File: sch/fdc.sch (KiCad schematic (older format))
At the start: 22 parts, among them X4 SLOT-34

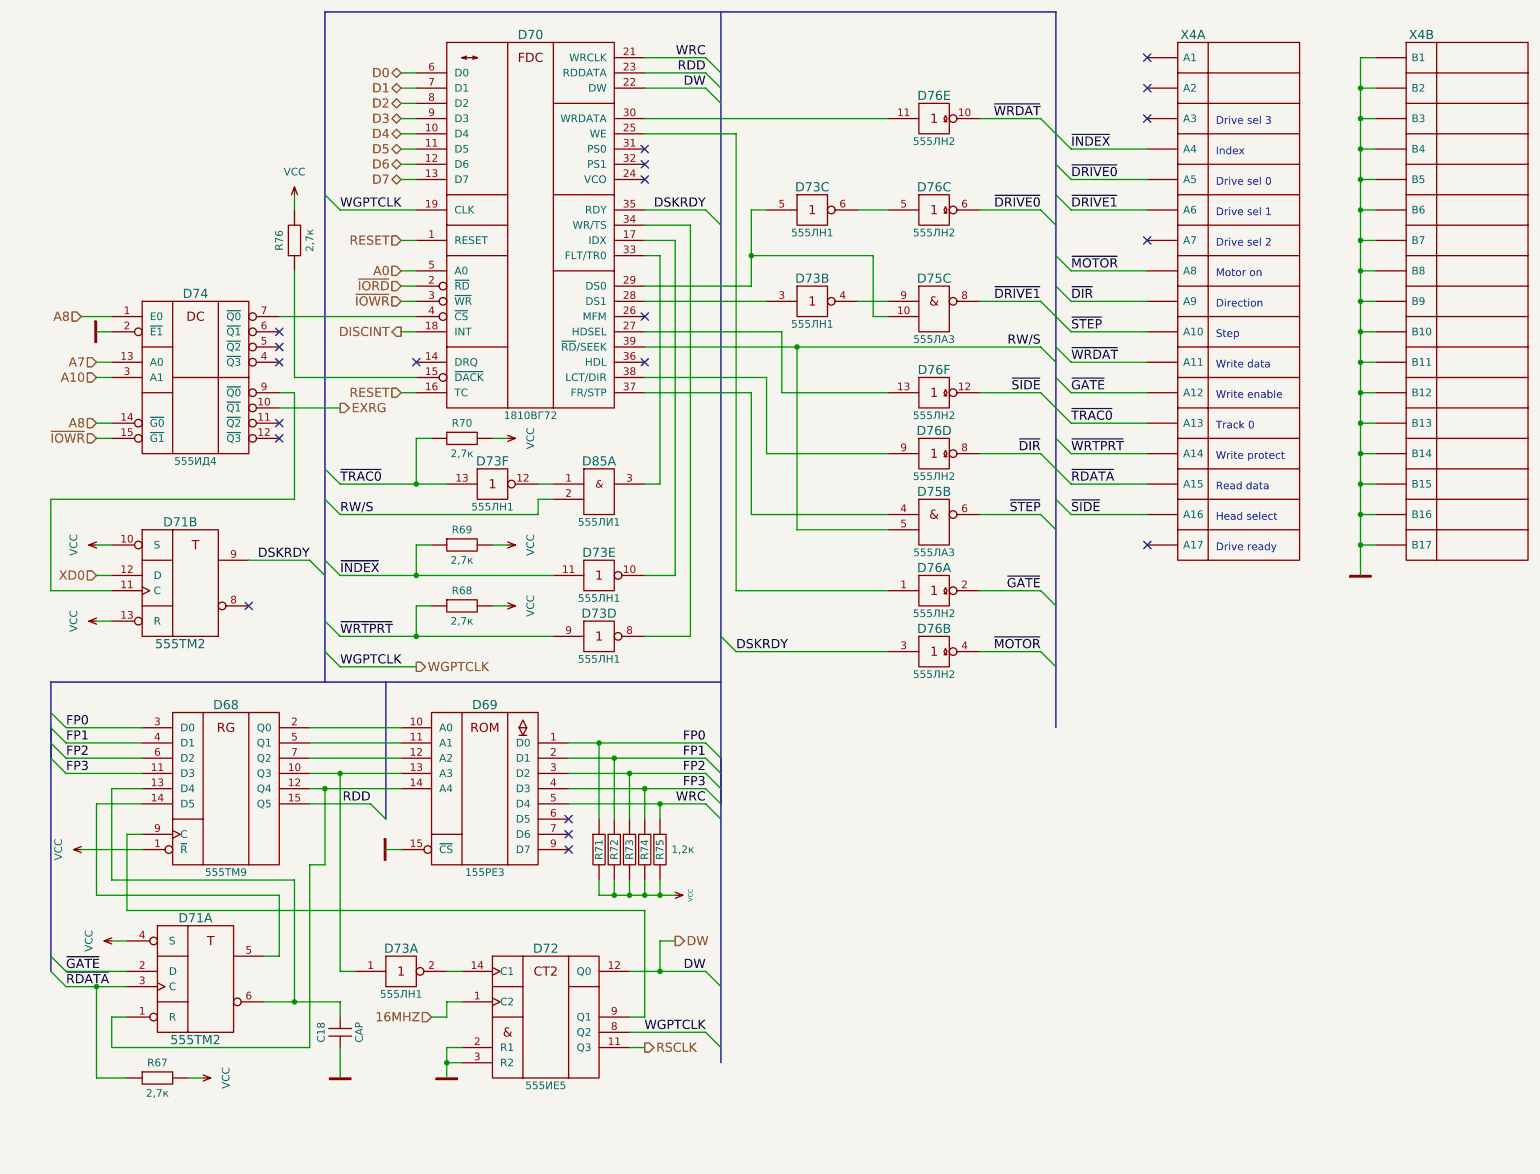
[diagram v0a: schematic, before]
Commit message: More precise version. PCB needs a lot of work.
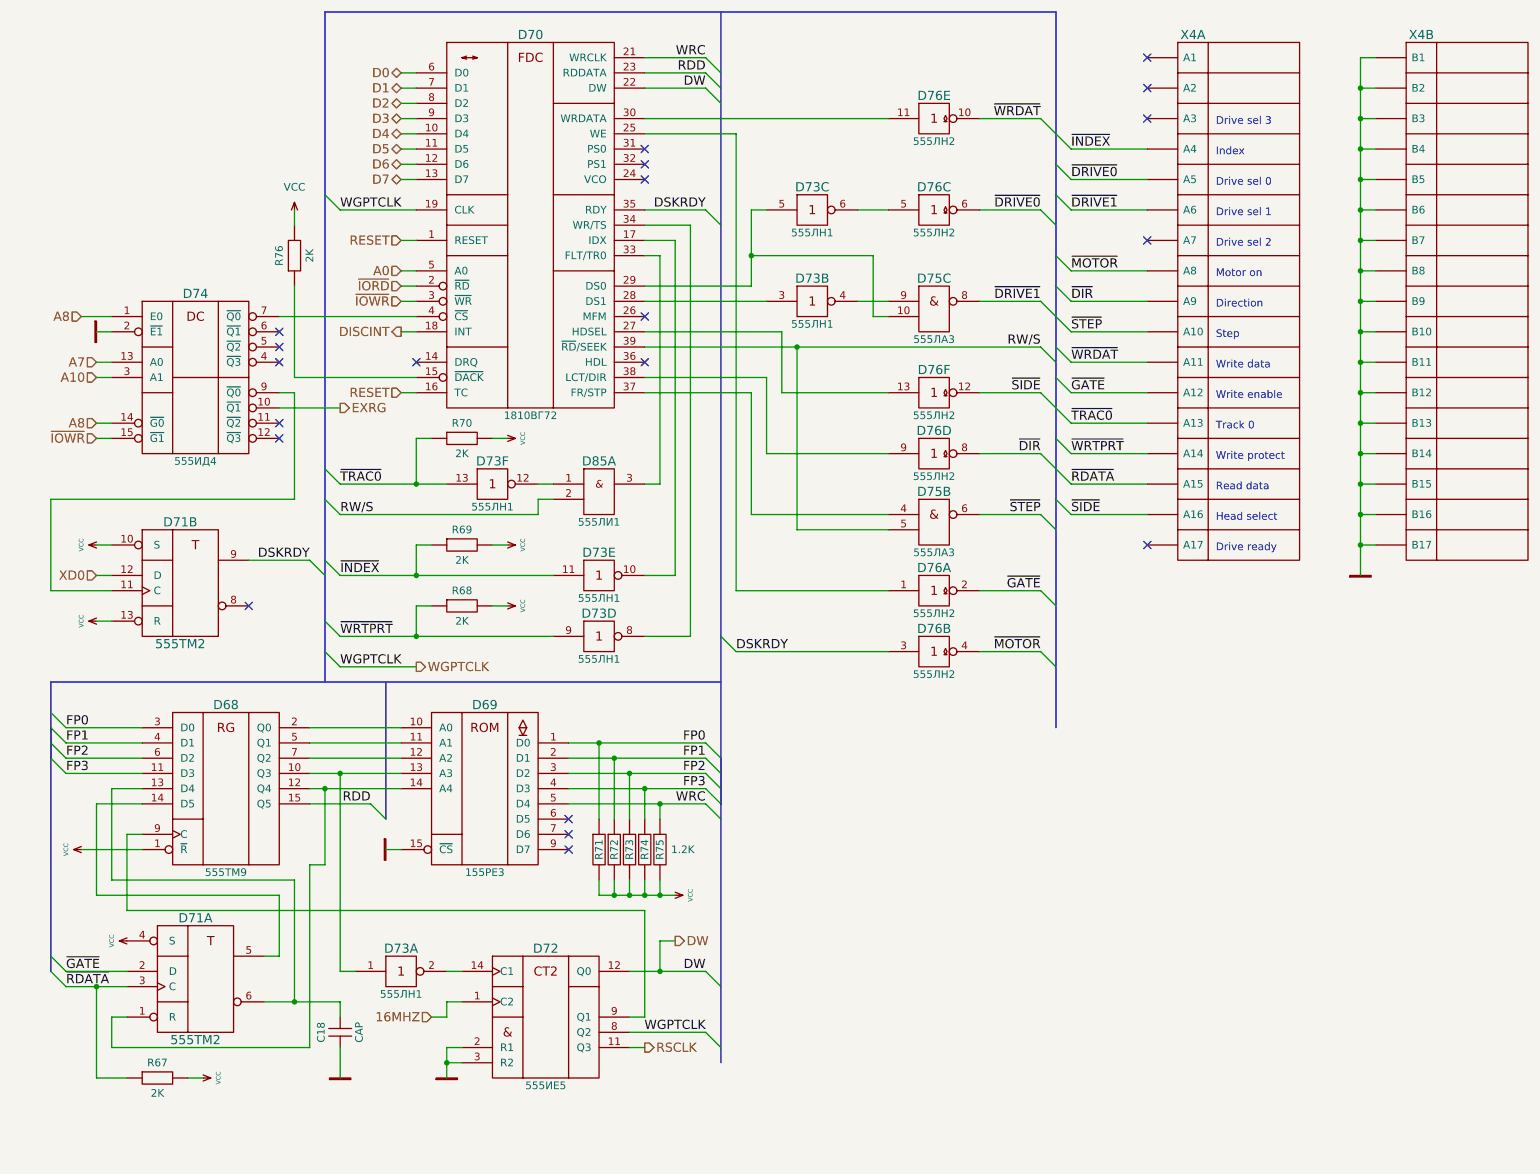
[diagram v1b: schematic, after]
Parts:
- C18: footprint MyLib:C_Disc_D7.5_P2.5 -> MyLib_metric:C_Disc_D7.5_P2.5
- D68, D69, D74: footprint MyLib:DIP-16 -> MyLib_metric:DIP-16
- D70: footprint MyLib:DIP-40 -> MyLib_metric:DIP-40
- D71, D72, D73, D75, D76, D85: footprint MyLib:DIP-14 -> MyLib_metric:DIP-14
- R67, R68, R69, R70: value 2,7к -> 2K; footprint MyLib:Resistor_Vertical_RM2.5mm -> MyLib_metric:Resistor_Vertical_RM2.5mm
- R71, R72, R73, R74, R75: value 1,2к -> 1.2K; footprint MyLib:Resistor_Vertical_RM2.5mm -> MyLib_metric:Resistor_Vertical_RM2.5mm
- R76: value 2,7к -> 2K; footprint MyLib:Resistor_Horizontal_RM7.5mm -> MyLib_metric:Resistor_Horizontal_RM7.5mm
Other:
- moved on the sheet: R76

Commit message: IR22 and IR23 symbols updated, part values updated
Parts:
- R67, R68, R69, R70, R76: value 2K -> 2,7к
- R71, R72, R73, R74, R75: value 1.2K -> 1,2к
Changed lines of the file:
@@
 P 4600 6100
 F 0 "R71" H 4600 6100 50  0000 C CNN
-F 1 "1.2K" H 4600 6000 50  0001 C CNN
+F 1 "1,2к" H 4600 6000 50  0001 C CNN
 F 2 "MyLib_metric:Resistor_Vertical_RM2.5mm" H 4600 6050 60  0001 C CNN
 F 3 "" H 4600 6050 60  0000 C CNN
@@
 P 4700 6100
 F 0 "R72" H 4700 6100 50  0000 C CNN
-F 1 "1.2K" H 4700 6000 50  0001 C CNN
+F 1 "1,2к" H 4700 6000 50  0001 C CNN
 F 2 "MyLib_metric:Resistor_Vertical_RM2.5mm" H 4700 6050 60  0001 C CNN
 F 3 "" H 4700 6050 60  0000 C CNN
@@
 P 4800 6100
 F 0 "R73" H 4800 6100 50  0000 C CNN
-F 1 "1.2K" H 4800 6000 50  0001 C CNN
+F 1 "1,2к" H 4800 6000 50  0001 C CNN
 F 2 "MyLib_metric:Resistor_Vertical_RM2.5mm" H 4800 6050 60  0001 C CNN
 F 3 "" H 4800 6050 60  0000 C CNN
@@
 P 4900 6100
 F 0 "R74" H 4900 6100 50  0000 C CNN
-F 1 "1.2K" H 4900 6000 50  0001 C CNN
+F 1 "1,2к" H 4900 6000 50  0001 C CNN
 F 2 "MyLib_metric:Resistor_Vertical_RM2.5mm" H 4900 6050 60  0001 C CNN
 F 3 "" H 4900 6050 60  0000 C CNN
@@
 P 5000 6100
 F 0 "R75" H 5000 6100 50  0000 C CNN
-F 1 "1.2K" V 5000 5950 50  0000 C CNN
+F 1 "1,2к" V 5000 5950 50  0000 C CNN
 F 2 "MyLib_metric:Resistor_Vertical_RM2.5mm" H 5000 6050 60  0001 C CNN
 F 3 "" H 5000 6050 60  0000 C CNN
@@
 P 1700 7600
 F 0 "R67" H 1700 7700 50  0000 C CNN
-F 1 "2K" H 1700 7500 50  0000 C CNN
+F 1 "2,7к" H 1700 7500 50  0000 C CNN
 F 2 "MyLib_metric:Resistor_Vertical_RM2.5mm" H 1700 7550 60  0001 C CNN
 F 3 "" H 1700 7550 60  0000 C CNN
@@
 P 3700 4500
 F 0 "R68" H 3700 4600 50  0000 C CNN
-F 1 "2K" H 3700 4400 50  0000 C CNN
+F 1 "2,7к" H 3700 4400 50  0000 C CNN
 F 2 "MyLib_metric:Resistor_Vertical_RM2.5mm" H 3700 4450 60  0001 C CNN
 F 3 "" H 3700 4450 60  0000 C CNN
@@
 P 3700 4100
 F 0 "R69" H 3700 4200 50  0000 C CNN
-F 1 "2K" H 3700 4000 50  0000 C CNN
+F 1 "2,7к" H 3700 4000 50  0000 C CNN
 F 2 "MyLib_metric:Resistor_Vertical_RM2.5mm" H 3700 4050 60  0001 C CNN
 F 3 "" H 3700 4050 60  0000 C CNN
@@
 P 3700 3400
 F 0 "R70" H 3700 3500 50  0000 C CNN
-F 1 "2K" H 3700 3300 50  0000 C CNN
+F 1 "2,7к" H 3700 3300 50  0000 C CNN
 F 2 "MyLib_metric:Resistor_Vertical_RM2.5mm" H 3700 3350 60  0001 C CNN
 F 3 "" H 3700 3350 60  0000 C CNN
@@
 P 2600 2200
 F 0 "R76" H 2600 2300 50  0000 C CNN
-F 1 "2K" H 2600 2100 50  0000 C CNN
+F 1 "2,7к" H 2600 2100 50  0000 C CNN
 F 2 "MyLib_metric:Resistor_Horizontal_RM7.5mm" H 2600 2150 60  0001 C CNN
 F 3 "" H 2600 2150 60  0000 C CNN
